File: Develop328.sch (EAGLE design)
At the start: 12 parts, among them IC1 ATMEGA328P-PU

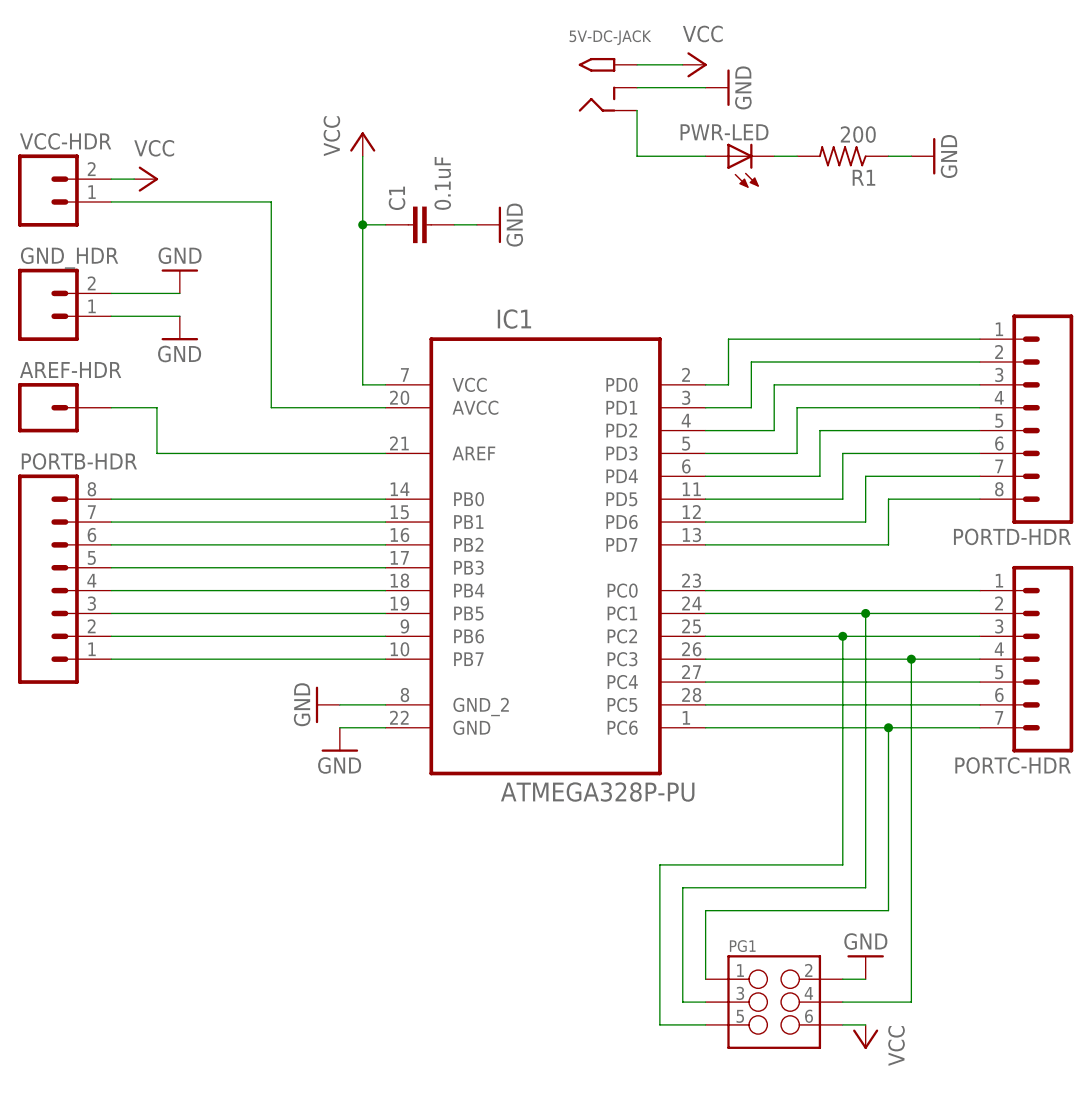
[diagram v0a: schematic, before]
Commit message: Fixed incorrect wiring for 6 pin programmer
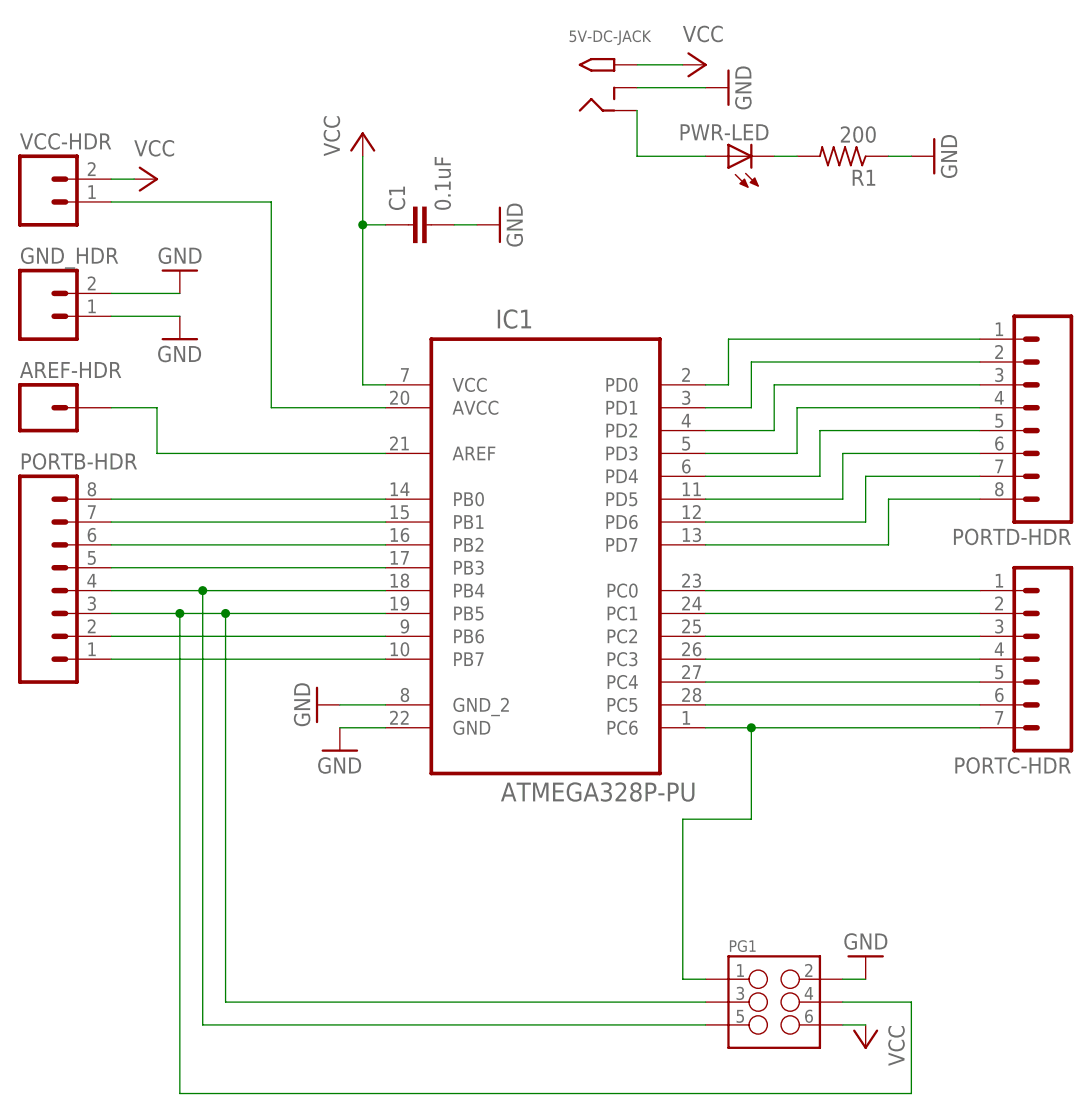
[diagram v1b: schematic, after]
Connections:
- removed net N$10: IC1.PC1, PG1.3, PORTC-HDR.2
- removed net N$11: IC1.PC2, PG1.5, PORTC-HDR.3
- new net N$28: IC1.PC2, PORTC-HDR.3
- new net N$29: IC1.PC1, PORTC-HDR.2
- net N$12: no longer PG1.4
- net N$5: now also PG1.5
- net N$6: now also PG1.3, PG1.4
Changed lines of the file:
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@@
 <pinref part="PORTB-HDR" gate="G$1" pin="4"/>
 <pinref part="IC1" gate="A" pin="PB4"/>
-<wire x1="17.78" y1="40.64" x2="48.26" y2="40.64" width="0.1524" layer="91"/>
+<wire x1="17.78" y1="40.64" x2="27.94" y2="40.64" width="0.1524" layer="91"/>
+<pinref part="PG1" gate="G$1" pin="5"/>
+<wire x1="27.94" y1="40.64" x2="48.26" y2="40.64" width="0.1524" layer="91"/>
+<wire x1="83.82" y1="-7.62" x2="27.94" y2="-7.62" width="0.1524" layer="91"/>
+<wire x1="27.94" y1="-7.62" x2="27.94" y2="40.64" width="0.1524" layer="91"/>
+<junction x="27.94" y="40.64"/>
 </segment>
 </net>
@@
 <pinref part="PORTB-HDR" gate="G$1" pin="3"/>
 <pinref part="IC1" gate="A" pin="PB5"/>
-<wire x1="17.78" y1="38.1" x2="48.26" y2="38.1" width="0.1524" layer="91"/>
+<wire x1="17.78" y1="38.1" x2="25.4" y2="38.1" width="0.1524" layer="91"/>
+<pinref part="PG1" gate="G$1" pin="4"/>
+<wire x1="25.4" y1="38.1" x2="30.48" y2="38.1" width="0.1524" layer="91"/>
+<wire x1="30.48" y1="38.1" x2="48.26" y2="38.1" width="0.1524" layer="91"/>
+<wire x1="99.06" y1="-5.08" x2="106.68" y2="-5.08" width="0.1524" layer="91"/>
+<wire x1="106.68" y1="-5.08" x2="106.68" y2="-15.24" width="0.1524" layer="91"/>
+<wire x1="106.68" y1="-15.24" x2="25.4" y2="-15.24" width="0.1524" layer="91"/>
+<wire x1="25.4" y1="-15.24" x2="25.4" y2="38.1" width="0.1524" layer="91"/>
+<junction x="25.4" y="38.1"/>
+<pinref part="PG1" gate="G$1" pin="3"/>
+<wire x1="83.82" y1="-5.08" x2="30.48" y2="-5.08" width="0.1524" layer="91"/>
+<wire x1="30.48" y1="-5.08" x2="30.48" y2="38.1" width="0.1524" layer="91"/>
+<junction x="30.48" y="38.1"/>
 </segment>
 </net>
@@
 </segment>
 </net>
-<net name="N$10" class="0">
-<segment>
-<pinref part="PORTC-HDR" gate="G$1" pin="2"/>
-<pinref part="IC1" gate="A" pin="PC1"/>
-<wire x1="114.3" y1="38.1" x2="101.6" y2="38.1" width="0.1524" layer="91"/>
-<pinref part="PG1" gate="G$1" pin="3"/>
-<wire x1="101.6" y1="38.1" x2="83.82" y2="38.1" width="0.1524" layer="91"/>
-<wire x1="83.82" y1="-5.08" x2="81.28" y2="-5.08" width="0.1524" layer="91"/>
-<wire x1="81.28" y1="-5.08" x2="81.28" y2="7.62" width="0.1524" layer="91"/>
-<wire x1="81.28" y1="7.62" x2="101.6" y2="7.62" width="0.1524" layer="91"/>
-<wire x1="101.6" y1="7.62" x2="101.6" y2="38.1" width="0.1524" layer="91"/>
-<junction x="101.6" y="38.1"/>
-</segment>
-</net>
-<net name="N$11" class="0">
-<segment>
-<pinref part="PORTC-HDR" gate="G$1" pin="3"/>
-<pinref part="IC1" gate="A" pin="PC2"/>
-<wire x1="114.3" y1="35.56" x2="99.06" y2="35.56" width="0.1524" layer="91"/>
-<pinref part="PG1" gate="G$1" pin="5"/>
-<wire x1="99.06" y1="35.56" x2="83.82" y2="35.56" width="0.1524" layer="91"/>
-<wire x1="83.82" y1="-7.62" x2="78.74" y2="-7.62" width="0.1524" layer="91"/>
-<wire x1="78.74" y1="-7.62" x2="78.74" y2="10.16" width="0.1524" layer="91"/>
-<wire x1="78.74" y1="10.16" x2="99.06" y2="10.16" width="0.1524" layer="91"/>
-<wire x1="99.06" y1="10.16" x2="99.06" y2="35.56" width="0.1524" layer="91"/>
-<junction x="99.06" y="35.56"/>
-</segment>
-</net>
 <net name="N$12" class="0">
 <segment>
 <pinref part="PORTC-HDR" gate="G$1" pin="4"/>
 <pinref part="IC1" gate="A" pin="PC3"/>
-<wire x1="114.3" y1="33.02" x2="106.68" y2="33.02" width="0.1524" layer="91"/>
-<pinref part="PG1" gate="G$1" pin="4"/>
-<wire x1="106.68" y1="33.02" x2="83.82" y2="33.02" width="0.1524" layer="91"/>
-<wire x1="99.06" y1="-5.08" x2="106.68" y2="-5.08" width="0.1524" layer="91"/>
-<wire x1="106.68" y1="-5.08" x2="106.68" y2="33.02" width="0.1524" layer="91"/>
-<junction x="106.68" y="33.02"/>
+<wire x1="114.3" y1="33.02" x2="83.82" y2="33.02" width="0.1524" layer="91"/>
 </segment>
 </net>
@@
 <pinref part="PORTC-HDR" gate="G$1" pin="7"/>
 <pinref part="IC1" gate="A" pin="PC6"/>
-<wire x1="114.3" y1="25.4" x2="104.14" y2="25.4" width="0.1524" layer="91"/>
+<wire x1="114.3" y1="25.4" x2="88.9" y2="25.4" width="0.1524" layer="91"/>
 <pinref part="PG1" gate="G$1" pin="1"/>
-<wire x1="104.14" y1="25.4" x2="83.82" y2="25.4" width="0.1524" layer="91"/>
-<wire x1="83.82" y1="-2.54" x2="83.82" y2="5.08" width="0.1524" layer="91"/>
-<wire x1="83.82" y1="5.08" x2="104.14" y2="5.08" width="0.1524" layer="91"/>
-<wire x1="104.14" y1="5.08" x2="104.14" y2="25.4" width="0.1524" layer="91"/>
-<junction x="104.14" y="25.4"/>
+<wire x1="88.9" y1="25.4" x2="83.82" y2="25.4" width="0.1524" layer="91"/>
+<wire x1="83.82" y1="-2.54" x2="81.28" y2="-2.54" width="0.1524" layer="91"/>
+<wire x1="81.28" y1="-2.54" x2="81.28" y2="15.24" width="0.1524" layer="91"/>
+<wire x1="81.28" y1="15.24" x2="88.9" y2="15.24" width="0.1524" layer="91"/>
+<wire x1="88.9" y1="15.24" x2="88.9" y2="25.4" width="0.1524" layer="91"/>
+<junction x="88.9" y="25.4"/>
 </segment>
 </net>
@@
 </segment>
 </net>
+<net name="N$28" class="0">
+<segment>
+<pinref part="IC1" gate="A" pin="PC2"/>
+<pinref part="PORTC-HDR" gate="G$1" pin="3"/>
+<wire x1="114.3" y1="35.56" x2="83.82" y2="35.56" width="0.1524" layer="91"/>
+</segment>
+</net>
+<net name="N$29" class="0">
+<segment>
+<pinref part="IC1" gate="A" pin="PC1"/>
+<pinref part="PORTC-HDR" gate="G$1" pin="2"/>
+<wire x1="114.3" y1="38.1" x2="83.82" y2="38.1" width="0.1524" layer="91"/>
+</segment>
+</net>
